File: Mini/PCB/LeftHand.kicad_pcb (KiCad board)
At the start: 2 copper layers, 155.9 x 99.3 mm, 0 parts

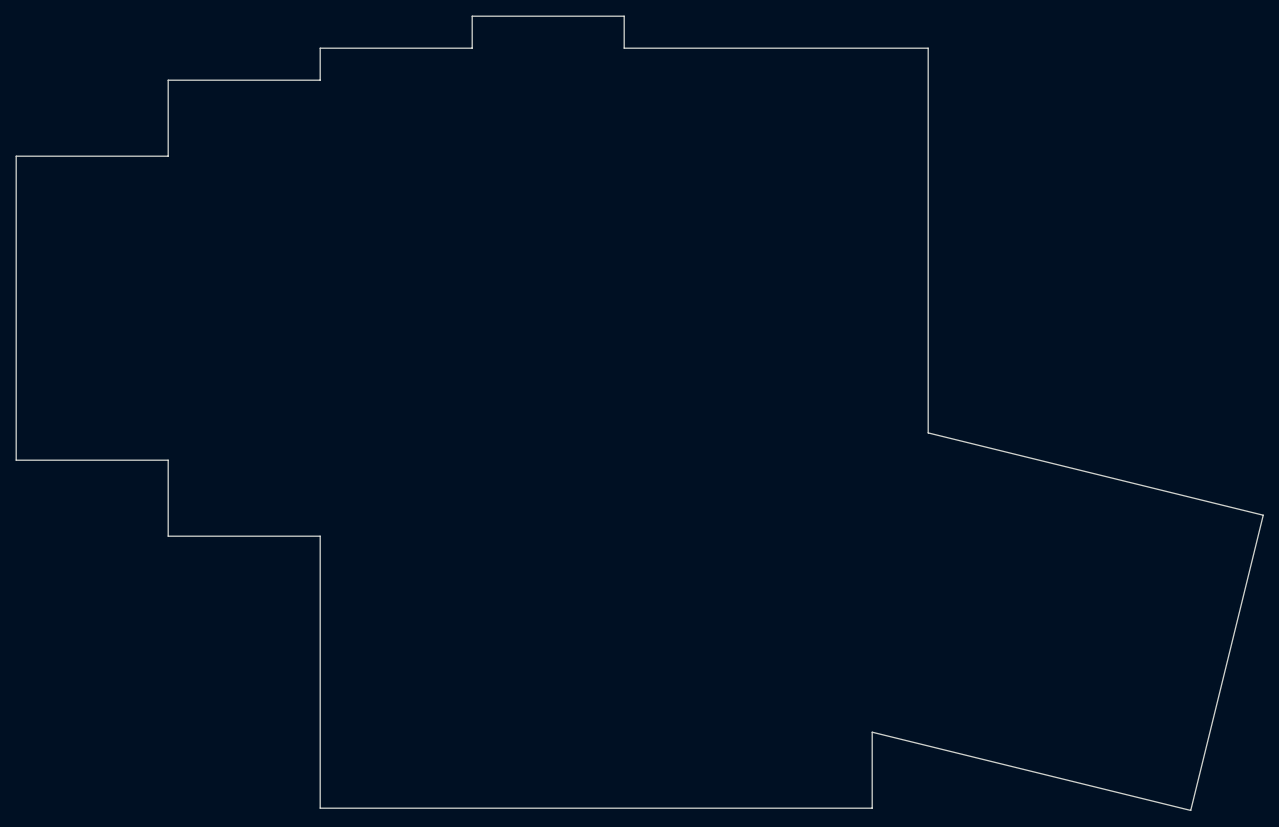
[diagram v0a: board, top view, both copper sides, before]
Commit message: Adding components to PCB.  Fixing T2 footprints.  Still need wiring and holes.
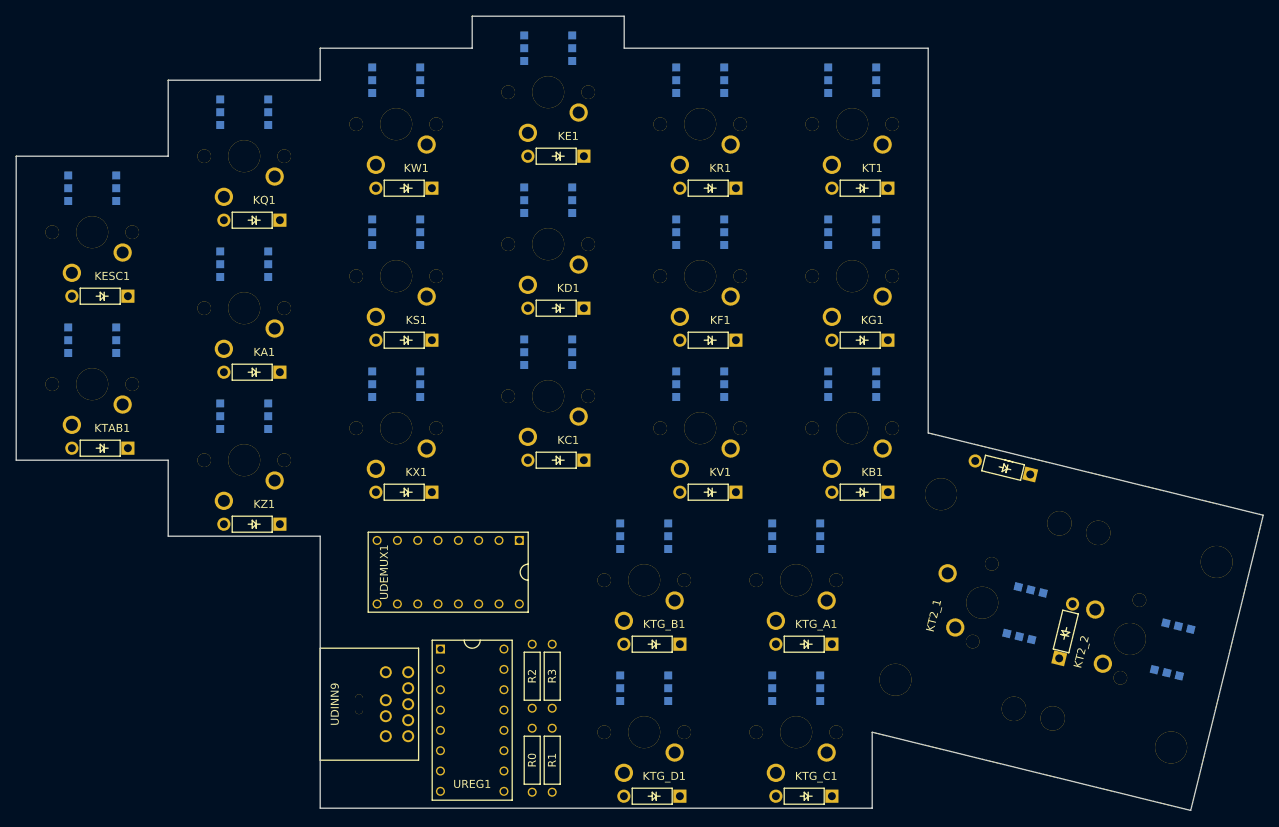
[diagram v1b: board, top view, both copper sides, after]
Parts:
- added KA1: KeyLedDiode, Mini:KeyLedDiodeR2L, F.Cu at (40.5, 48.5)
- added KB1: KeyLedDiode, Mini:KeyLedDiodeL2R, F.Cu at (116.5, 63.5)
- added KC1: KeyLedDiode, Mini:KeyLedDiodeL2R, F.Cu at (78.5, 59.5)
- added KD1: KeyLedDiode, Mini:KeyLedDiodeR2L, F.Cu at (78.5, 40.5)
- added KE1: KeyLedDiode, Mini:KeyLedDiodeL2R, F.Cu at (78.5, 21.5)
- added KESC1: KeyLedDiode, Mini:KeyLedDiodeL2R, F.Cu at (21.5, 39.0)
- added KF1: KeyLedDiode, Mini:KeyLedDiodeR2L, F.Cu at (97.5, 44.5)
- added KG1: KeyLedDiode, Mini:KeyLedDiodeR2L, F.Cu at (116.5, 44.5)
- added KQ1: KeyLedDiode, Mini:KeyLedDiodeL2R, F.Cu at (40.5, 29.5)
- added KR1: KeyLedDiode, Mini:KeyLedDiodeL2R, F.Cu at (97.5, 25.5)
- added KS1: KeyLedDiode, Mini:KeyLedDiodeR2L, F.Cu at (59.5, 44.5)
- added KT1: KeyLedDiode, Mini:KeyLedDiodeL2R, F.Cu at (116.5, 25.5)
- added KT2_1: KeyLedDiode, Mini:Key2LedDiodeL2R, F.Cu at (132.8, 85.3)
- added KT2_2: KeyLedDiode, Mini:Key2LedDiodeR2L, F.Cu at (151.2, 89.8)
- added KTAB1: KeyLedDiode, Mini:KeyLedDiodeR2L, F.Cu at (21.5, 58.0)
- added KTG_A1: KeyLedDiode, Mini:KeyLedDiodeR2L, F.Cu at (109.5, 82.5)
- added KTG_B1: KeyLedDiode, Mini:KeyLedDiodeR2L, F.Cu at (90.5, 82.5)
- added KTG_C1: KeyLedDiode, Mini:KeyLedDiodeL2R, F.Cu at (109.5, 101.5)
- added KTG_D1: KeyLedDiode, Mini:KeyLedDiodeL2R, F.Cu at (90.5, 101.5)
- added KV1: KeyLedDiode, Mini:KeyLedDiodeL2R, F.Cu at (97.5, 63.5)
- added KW1: KeyLedDiode, Mini:KeyLedDiodeL2R, F.Cu at (59.5, 25.5)
- added KX1: KeyLedDiode, Mini:KeyLedDiodeL2R, F.Cu at (59.5, 63.5)
- added KZ1: KeyLedDiode, Mini:KeyLedDiodeL2R, F.Cu at (40.5, 67.5)
- added R0: R, Mini:PullupResistor, F.Cu at (76.5, 105.0)
- added R1: R, Mini:PullupResistor, F.Cu at (79.0, 105.0)
- added R2: R, Mini:PullupResistor, F.Cu at (76.5, 94.5)
- added R3: R, Mini:PullupResistor, F.Cu at (79.0, 94.5)
- added UDEMUX1: Demultiplexer, Mini:DualInlineMicrochip2x8, F.Cu at (66.0, 81.5)
- added UDINN9: MiniDINN9, Mini:MiniDin9, F.Cu at (54.9, 98.0)
- added UREG1: ParallelLoadShiftRegister, Mini:DualInlineMicrochip2x8, F.Cu at (69.0, 100.0)

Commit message: Left hand edge cuts for LEDs and pegs.
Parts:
- turned UDEMUX1 to 90 degrees
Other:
- outline, holes or cut-outs redrawn

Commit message: Finished wiring left hand.  Generated gerber files.
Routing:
- net GND: track 0.00 -> 630.8 mm, vias 0 -> 31
- net VCC: track 0.00 -> 630.8 mm, vias 0 -> 14
- net C0: track 0.00 -> 200.4 mm, vias 0 -> 2
- net C2: track 0.00 -> 184.4 mm, vias 0 -> 3
- net C1: track 0.00 -> 182.9 mm, vias 0 -> 1
- net R2: track 0.00 -> 134.2 mm, vias 0 -> 3
- net S0_DL: track 0.00 -> 123.0 mm, vias 0 -> 3
- net R1: track 0.00 -> 122.5 mm, vias 0 -> 3
- net R0: track 0.00 -> 116.4 mm, vias 0 -> 4
- net CLK_L: track 0.00 -> 115.0 mm, vias 0 -> 6
- net R3: track 0.00 -> 105.3 mm, vias 0 -> 1
- net C3: track 0.00 -> 92.3 mm
- net R7: track 0.00 -> 80.7 mm, vias 0 -> 1
- net R6: track 0.00 -> 71.9 mm
- net R4: track 0.00 -> 61.6 mm, vias 0 -> 1
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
